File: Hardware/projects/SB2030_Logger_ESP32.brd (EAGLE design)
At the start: 36.5 x 80 mm, 34 parts, among them SW1 CKTACTSWITCH, U1 ESP-WROOM-32, U2 MCP2562, U3 NCP1117ST50T3G, U4 NCP1117ST33T3G, U5 SN65C1168PWR, X1 1751280

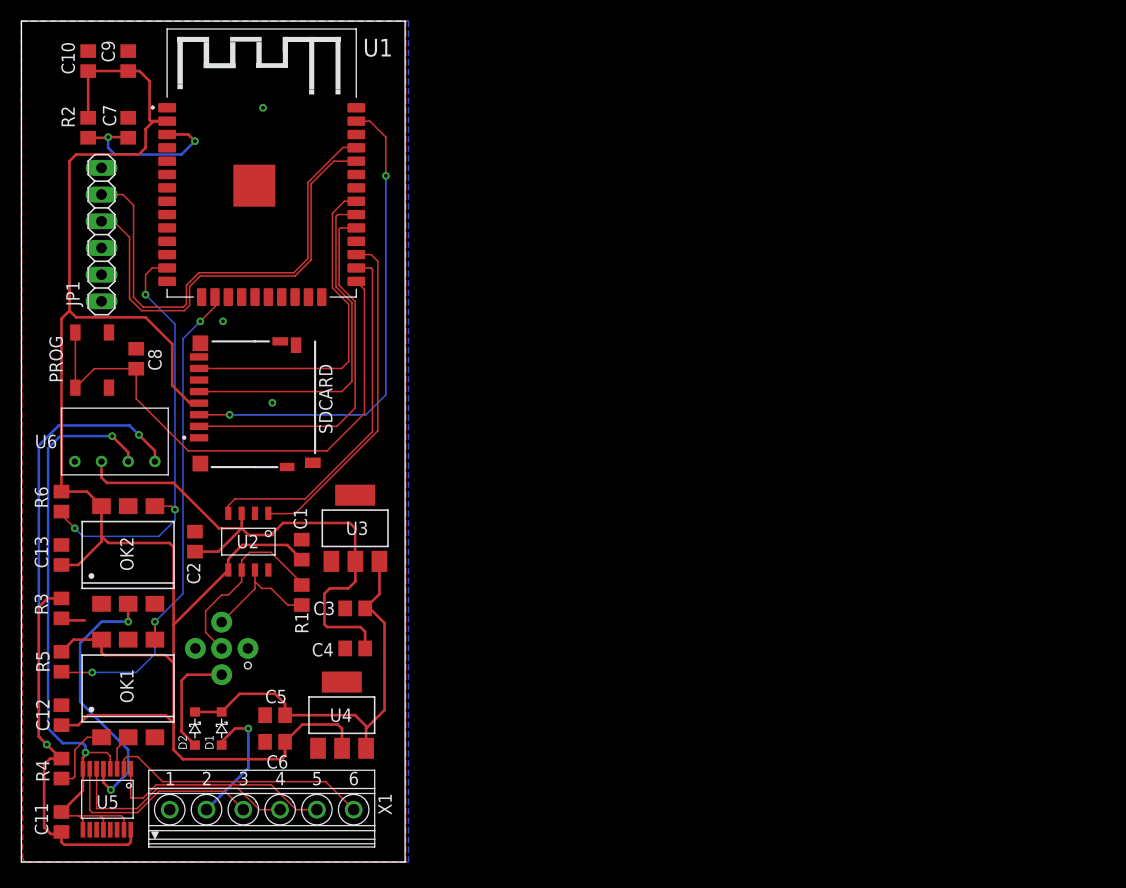
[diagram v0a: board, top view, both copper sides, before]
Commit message: Major updates to SMD board design (added motion sensor and power management), with re-layout for production. Added Gerbers, BOM, and CPL for JLCPCB production. Added library for MPU6050 IMU. Added CCOM logo for silkscreen.
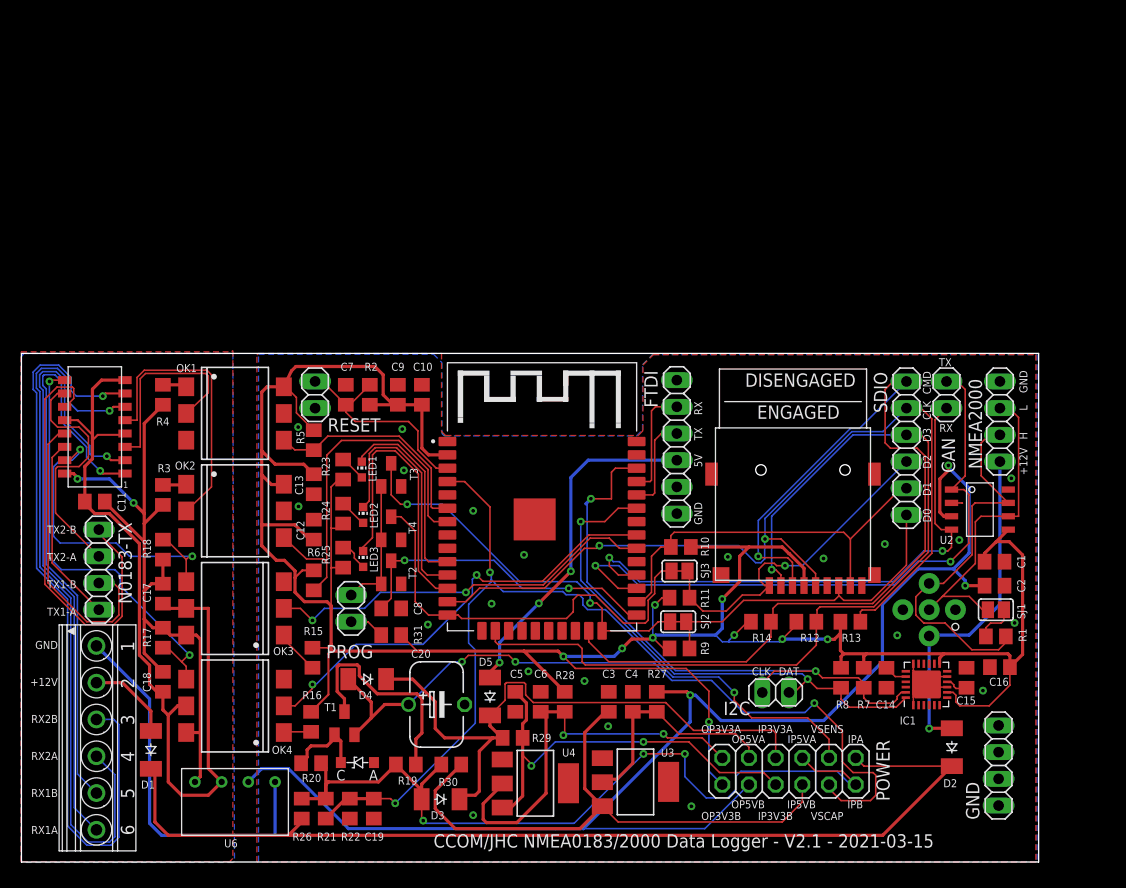
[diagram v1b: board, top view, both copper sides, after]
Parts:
- removed JP1: FTDI/ICSP, pinhead:1X06
- removed SDCARD: MicroSD Holder, 1140084168:1140084168
- removed SW1: CKTACTSWITCH, sb2030_logger:CKTACTSWITCH
- added C14: 2n2, rcl:C0805
- added C15, C17, C18, C19: 0.1u, rcl:C0805
- added C16: 10n, rcl:C0805
- added C20: 0.47F, rcl:P128-50
- added CAN: CAN-TEST, pinhead:1X02
- added D3, D4, D5: SS14, diode:SOD-123_MINI-SMA
- added DZL4734: (no value), sb2030_logger:SOD-123FL
- added FTDI: FTDI/ICSP, pinhead:1X06
- added GND: (no value), pinhead:1X04
- added I2C: I2C_TEST, pinhead:1X02
- added IC1: MPU6050, invensense:QFN50P400X400X95-25T265X275N
- added LED1, LED2, LED3: (no value), led:CHIP-LED0603
- added N0183-TX: TX_TEST, pinhead:1X04
- added NMEA2000: NMEA2000-2, pinhead:1X04
- added OK3, OK4: H11L1MS, optocoupler:DIL6-SMD
- added POWER: (no value), pinhead:2X06
- added PROG: PROG, pinhead:1X02
- added R10, R11, R12, R13, R14, R9: 47k, rcl:R0805
- added R15, R16: 560, rcl:R0805
- added R17, R18, R22, R7, R8: 10k, rcl:R0805
- added R19: 47R, rcl:R0805
- added R20: 1k, rcl:R0805
- added R21: 33k, rcl:R0805
- added R23, R24, R25: 220, rcl:R0805
- added R26, R27, R28, R29, R30: 1R, rcl:R0805
- added R31: 6k8, rcl:R0805
- added RESET: RESET, pinhead:1X02
- added SDIO: SDIO_TEST, pinhead:1X06
- added SJ1, SJ2, SJ3: (no value), jumper:SJ
- added T1: (no value), transistor:SOT23-BEC
- added T2, T3, T4: S8050, transistor:SOT23
- added U$1: MICRO-SD, sb2030_logger:XUNPU-MICROSD-SOCKET
- D1, D2: value 1N5819 -> SS14; device sb2030_logger:SOD123 -> diode:SOD-123_MINI-SMA
- R3, R4: value 1k2 -> 1k
- U3: value NCP1117ST50T3G -> AMS1117-5.0
- U4: value NCP1117ST33T3G -> AMS1117-3.3
- U5: device sb2030_logger:16-TSSOP -> sb2030_logger:SOIC16
- moved C2 76.2 mm to (92.6, 26.3), turned to 0 degrees
- moved D2 72.0 mm to (88.5, 10.9)
- moved U2 69.7 mm to (91.2, 33.5), turned to 270 degrees
- moved JP2 67.4 mm to (86.4, 24.0)
- moved R1 66.2 mm to (92.7, 21.5), turned to 0 degrees
- moved C1 65.9 mm to (92.6, 28.6), turned to 0 degrees
- moved C10 44.9 mm to (38.1, 44.5)
- moved U1 41.5 mm to (49.5, 31.8)
- moved C9 40.8 mm to (35.8, 44.5)
- moved R2 36.9 mm to (33.1, 44.5), turned to 270 degrees
- moved R4 36.8 mm to (13.5, 44.5), turned to 270 degrees
- moved U5 36.1 mm to (6.99, 42.0), turned to 180 degrees
- moved U3 36.0 mm to (58.4, 7.62), turned to 270 degrees
- moved C8 33.9 mm to (35.2, 24.1), turned to 0 degrees
- moved C7 32.8 mm to (30.9, 44.5)
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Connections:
- removed net VIN: C3.1, C5.1, D1.2, D2.2, U3.3, U4.3
- new net CAN-12V: D2.A, JP2.2, NMEA2000.1
- new net FTDI-5V: D5.A, FTDI.3
- new net IP_CUR_3V3_A: D3.C, D4.C, D5.C, POWER.7, R29.2
- new net IP_CUR_3V3_B: C5.1, POWER.8, R29.1, U4.3
- new net IP_CUR_5V_B: C3.1, POWER.6, R30.1, U3.3
- new net IP_CUR_A: D1.C, D2.C, POWER.1, R26.2
- new net IP_CUR_B: D3.A, POWER.2, POWER.5, R19.2, R20.2, R21.2, R26.1, R30.2
- new net N$11: R10.1, SDIO.2, U$1.8, U1.26
- new net N$23: C14.1, IC1.20
- new net N$24: R12.1, SDIO.4, U$1.2, U1.16
- new net N$25: R13.1, SDIO.5, U$1.5, U1.13
- new net N$26: R14.1, SDIO.6, U$1.3, U1.23
- new net N$27: N0183-TX.4, U5.1Y
- new net N$28: N0183-TX.3, U5.1Z
- new net N$29: N0183-TX.2, U5.2Y
- new net N$3: R1.1, SJ1.2
- new net N$30: N0183-TX.1, U5.2Z
- new net N$31: OK3.1, R15.1
- new net N$32: OK4.1, R16.1
- new net N$33: OK3.4, R18.1, U5.1D
- new net N$34: OK4.4, R17.1, U5.2D
- new net N$35: LED1.C, U1.10
- new net N$36: LED2.C, U1.11
- new net N$37: PROG.2, T2.1, T3.1, T4.1
- new net N$38: LED3.C, U1.12
- new net N$39: LED1.A, R23.2
- new net N$40: LED2.A, R24.2
- new net N$41: DZL4734.K, R20.1, T1.B
- new net N$42: R19.1, T1.C
- new net N$43: PROG.1, R31.1
- new net N$44: LED3.A, R25.2
- new net OP_CUR_3V3_A: C6.1, POWER.11, R28.2, U4.2
- new net OP_CUR_5V_A: C4.1, POWER.9, R27.2, U3.2
- new net SCAP: C20.+, D4.A, POWER.4, T1.E
- new net TX1: OK3.2, U1.30
- new net TX2: OK4.2, U1.31
- new net VSENSE: C19.1, POWER.3, R21.1, R22.2, U1.4
- net +12V: now also D1.A; no longer D1.1
- net +3V3: now also C16.1, IC1.13, IC1.8, POWER.12, R10.2, R11.2, R12.2, R13.2, R14.2, R15.2, R16.2, R23.1, R24.1, R25.1, R28.1, R31.2, R7.2, R8.2, R9.2, U$1.4; no longer C6.1, SDCARD.4, U4.2
- net +5V: now also POWER.10, R27.1; no longer C4.1, U3.2
- net GND: now also C14.2, C15.2, C16.2, C19.2, C20.-, DZL4734.A, FTDI.1, GND.1, GND.2, GND.3, GND.4, IC1.1, IC1.11, IC1.18, IC1.25, IC1.9, NMEA2000.4, R22.1, RESET.2, T2.2, T3.2, T4.2, U$1.6, U$1.GND1, U$1.GND2, U$1.GND3, U$1.GND4; no longer JP1.1, SDCARD.6, SW1.3, SW1.4
- net GNDI: now also C17.2, C18.2, OK3.5, OK4.5, U5.1DE, U5.2DE, U5.GND; no longer U5.12, U5.15, U5.4, U5.8, U5.9
- net N$1: now also NMEA2000.2, R1.2; no longer R1.1
- net N$10: now also R11.1, SDIO.3, SJ3.1, SJ3.2, T4.3, U$1.1, U1.14; no longer SDCARD.7, U1.31
- net N$12: now also T2.3; no longer SW1.1, SW1.2
- net N$13: now also U5.1R; no longer U5.3
- net N$14: now also U5.2R; no longer U5.5
- net N$17: now also U5.1A; no longer U5.2
- net N$18: now also U5.1B; no longer U5.1
- net N$19: now also U5.2A; no longer U5.6
- net N$2: now also NMEA2000.3, SJ1.1; no longer R1.2
- net N$20: now also U5.2B; no longer U5.7
- net N$21: now also C17.1, C18.1, OK3.6, OK4.6, R17.2, R18.2, U5.VCC; no longer U5.16
- net N$22: now also R9.1, SDIO.1, SJ2.1, SJ2.2, T3.3, U$1.7, U1.24; no longer D2.1, JP2.2
- net N$4: now also RESET.1
- net N$5: now also I2C.2, IC1.23, R7.1, U1.36; no longer SDCARD.2, U1.29
- net N$6: now also CAN.2
- net N$7: now also CAN.1, U1.28; no longer U1.26
- net N$8: now also I2C.1, IC1.24, R8.1, U1.33; no longer SDCARD.3, U1.37
- net N$9: now also C15.1, IC1.10; no longer SDCARD.5, U1.30
- net RX1: now also U1.6; no longer U1.16
- net RX2: now also U1.7; no longer U1.13
- net RXDATA: now also FTDI.5; no longer JP1.5
- net TXDATA: now also FTDI.4; no longer JP1.4
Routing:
- net IP_CUR_A: track 0.00 -> 95.9 mm
- net +3V3: track 178.4 -> 272.7 mm, vias 0 -> 9
- net N$26: track 0.00 -> 89.1 mm, vias 0 -> 1
- net N$25: track 0.00 -> 87.9 mm, vias 0 -> 2
- net N$24: track 0.00 -> 86.3 mm, vias 0 -> 1
- net VSENSE: track 0.00 -> 86.2 mm, vias 0 -> 3
- net IP_CUR_B: track 0.00 -> 80.6 mm, vias 0 -> 3
- net +5V: track 52.6 -> 131.6 mm, vias 0 -> 3
- net SCAP: track 0.00 -> 71.9 mm, vias 0 -> 3
- net N$22: track 10.7 -> 70.5 mm, vias 0 -> 2
- net IP_CUR_3V3_A: track 0.00 -> 59.6 mm
- net IP_CUR_5V_B: track 0.00 -> 55.7 mm
- net N$20: track 20.2 -> 74.6 mm, vias 0 -> 1
- net GND: track 0.00 -> 48.5 mm, vias 3 -> 21
- net N$19: track 22.9 -> 69.5 mm, vias 0 -> 1
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- added copper zone on layer 1, net GNDI
- added copper zone on layer 16, net GNDI
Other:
- board size 36.5 x 80 mm -> 96.8 x 48.4 mm
- board text added: "(c) 2021 Center for Coastal and Ocean Mapping University of New Hampshire 2021-03-15 V2.1"
- board text added: "+12V"
- board text added: "5V"
- board text added: "CCOM/JHC NMEA0183/2000 Data Logger - V2.1 - 2021-03-15"
- board text added: "CLK"
- board text added: "CMD"
- board text added: "D0"
- board text added: "D1"
- board text added: "D2"
- board text added: "D3"
- board text added: "DAT"
- board text added: "GND"
- board text added: "H"
- board text added: "IP3V3A"
- board text added: "IP3V3B"
- board text added: "IP5VA"
- board text added: "IP5VB"
- board text added: "IPA"
- board text added: "IPB"
- board text added: "L"
- board text added: "OP3V3A"
- board text added: "OP3V3B"
- board text added: "OP5VA"
- board text added: "OP5VB"
- board text added: "RX"
- board text added: "RX1A"
- board text added: "RX1B"
- board text added: "RX2A"
- board text added: "RX2B"
- board text added: "TX"
- board text added: "TX1-A"
- board text added: "TX1-B"
- board text added: "TX2-A"
- board text added: "TX2-B"
- board text added: "VSCAP"
- board text added: "VSENS"
- board text removed: "PROG"

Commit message: Re-routed demonstration board to ensure that the power distribution is better.
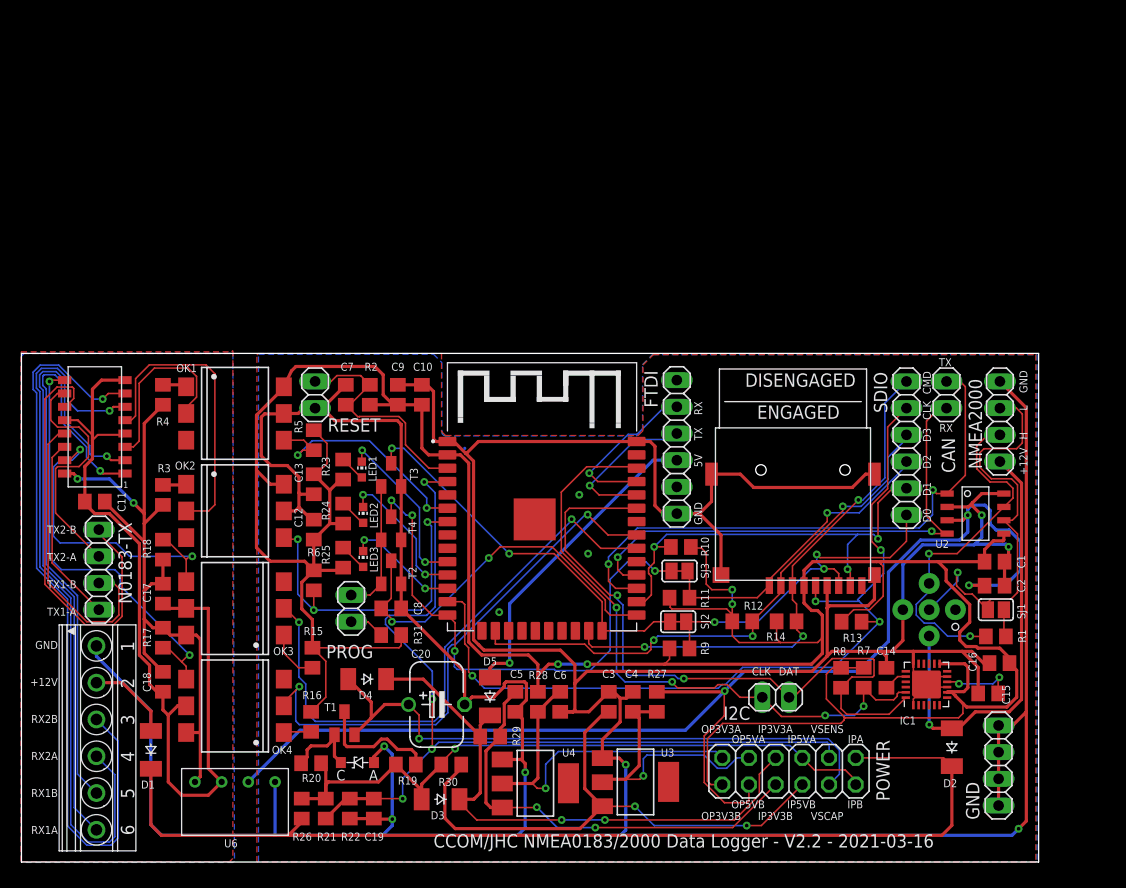
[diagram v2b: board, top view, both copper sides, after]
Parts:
- moved R12 6.10 mm to (68.6, 22.9)
- moved R28 2.55 mm to (49.1, 15.2)
- moved C15 2.54 mm to (92.0, 16.0), turned to 180 degrees
- moved R14 2.44 mm to (72.8, 22.9)
- moved R29 2.14 mm to (44.6, 11.9)
- moved C6 1.85 mm to (51.3, 15.2), turned to 270 degrees
- moved U2 0.57 mm to (90.8, 33.1)
- moved I2C 0.46 mm to (71.8, 15.7)
- moved C16 0.38 mm to (93.1, 18.9)
- moved R13 0.11 mm to (79.0, 22.9)
- turned C14 to 90 degrees
- turned R1 to 180 degrees
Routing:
- net GND: track 48.5 -> 497.2 mm, vias 21 -> 10
- net N$26: track 89.1 -> 51.6 mm, vias 1 -> 3
- net N$24: track 86.3 -> 53.4 mm, vias 1 -> 3
- net +3V3: track 272.7 -> 301.8 mm, vias 9 -> 4
- net TX1: track 37.7 -> 55.4 mm
- net N$38: track 27.6 -> 10.9 mm, vias 0 -> 2
- net IP_CUR_B: track 80.6 -> 65.2 mm, vias 3 -> 1
- net N$8: track 50.7 -> 65.3 mm
- net SCAP: track 71.9 -> 58.7 mm, vias 3 -> 1
- net N$2: track 30.9 -> 40.8 mm, vias 0 -> 1
- net CAN-12V: track 32.5 -> 42.2 mm
- net N$36: track 23.4 -> 13.9 mm, vias 0 -> 2
- net TX2: track 41.9 -> 51.1 mm
- net N$42: track 21.0 -> 11.9 mm
- net N$6: track 61.4 -> 54.5 mm
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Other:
- board text added: "CCOM/JHC NMEA0183/2000 Data Logger - V2.2 - 2021-03-16"
- board text removed: "CCOM/JHC NMEA0183/2000 Data Logger - V2.1 - 2021-03-15"

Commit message: Updates to library specifications for devices, and schematic/board to match in order to give better match to actual components; V2.3 of demonstration board.
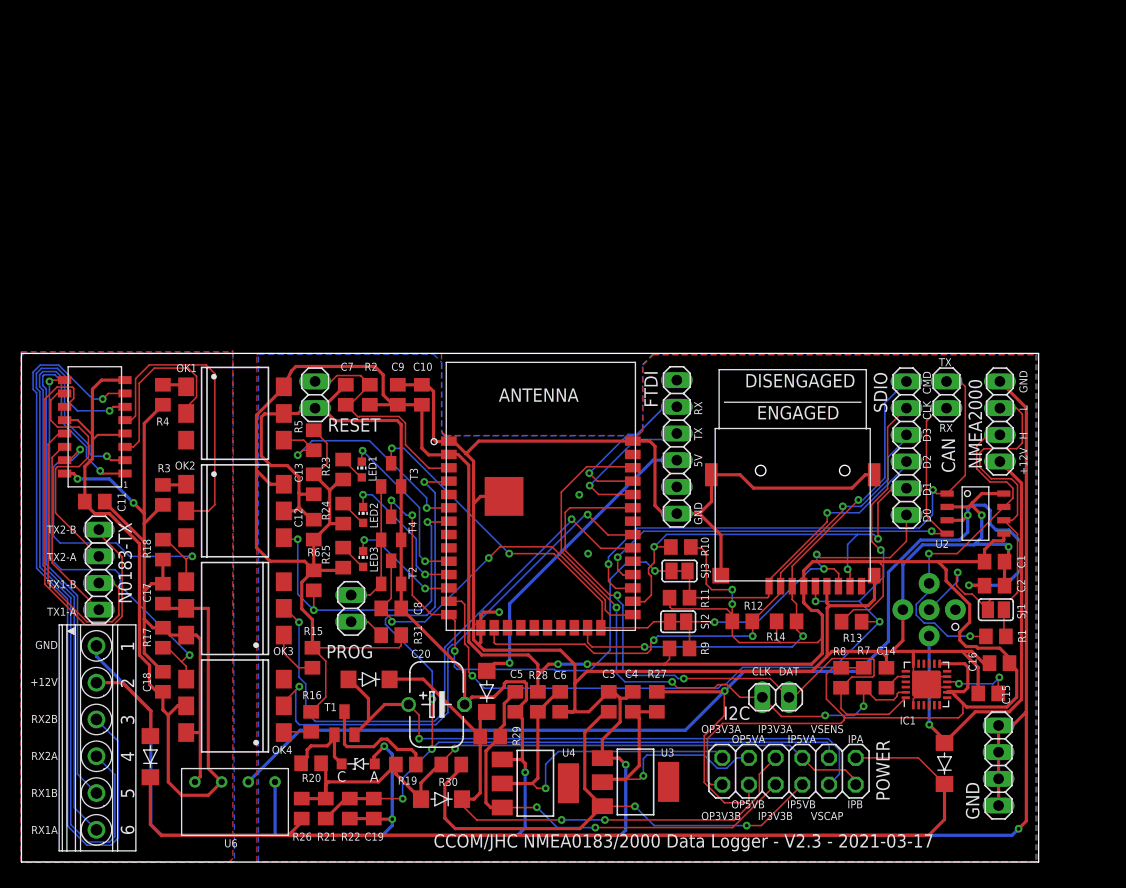
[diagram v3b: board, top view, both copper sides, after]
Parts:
- removed DZL4734: (no value), sb2030_logger:SOD-123FL
- removed U$1: MICRO-SD, sb2030_logger:XUNPU-MICROSD-SOCKET
- added H1: TF-115, sb2030_logger:XUNPU-MICROSD-SOCKET
- added Z1: DZL4734, sb2030_logger:SOD-123FL
- D1, D2, D3, D4, D5: device diode:SOD-123_MINI-SMA -> sb2030_logger:DO-214AC
- U1: value ESP-WROOM-32 -> ESP32-WROOM-32E; device ESP-WROOM-32:MODULE_ESP-WROOM-32 -> sb2030_logger:ESPS32-WROOM-32E
- U2: value MCP2562 -> TLA1051T/3
- moved U1 3.04 mm to (49.4, 34.8)
- moved D2 1.70 mm to (87.8, 9.37)
- moved D1 0.65 mm to (12.3, 10.0)
- moved D5 0.57 mm to (44.3, 16.2)
- moved D4 0.18 mm to (33.1, 17.4)
- moved D3 0.09 mm to (40.0, 5.98)
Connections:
- net +3V3: now also H1.4; no longer U$1.4
- net GND: now also H1.6, H1.GND1, H1.GND2, H1.GND3, H1.GND4, U1.THERM, Z1.A; no longer DZL4734.A, U$1.6, U$1.GND1, U$1.GND2, U$1.GND3, U$1.GND4, U1.1.1
- net IP_CUR_3V3_A: now also D3.K, D4.K, D5.K; no longer D3.C, D4.C, D5.C
- net IP_CUR_A: now also D1.K, D2.K; no longer D1.C, D2.C
- net N$10: now also H1.1; no longer U$1.1
- net N$11: now also H1.8; no longer U$1.8
- net N$22: now also H1.7; no longer U$1.7
- net N$24: now also H1.2; no longer U$1.2
- net N$25: now also H1.5; no longer U$1.5
- net N$26: now also H1.3; no longer U$1.3
- net N$41: now also Z1.K; no longer DZL4734.K
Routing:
- net GND: track 497.2 -> 505.1 mm
- net IP_CUR_A: track 99.6 -> 96.0 mm
- net CAN-12V: track 42.2 -> 43.3 mm
- net N$10: track 81.7 -> 82.4 mm
- net +12V: track 8.19 -> 8.70 mm
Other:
- board text added: "(c) 2021 Center for Coastal and Ocean Mapping University of New Hampshire 2021-03-17 V2.3"
- board text added: "CCOM/JHC NMEA0183/2000 Data Logger - V2.3 - 2021-03-17"
- board text removed: "(c) 2021 Center for Coastal and Ocean Mapping University of New Hampshire 2021-03-15 V2.1"
- board text removed: "CCOM/JHC NMEA0183/2000 Data Logger - V2.2 - 2021-03-16"

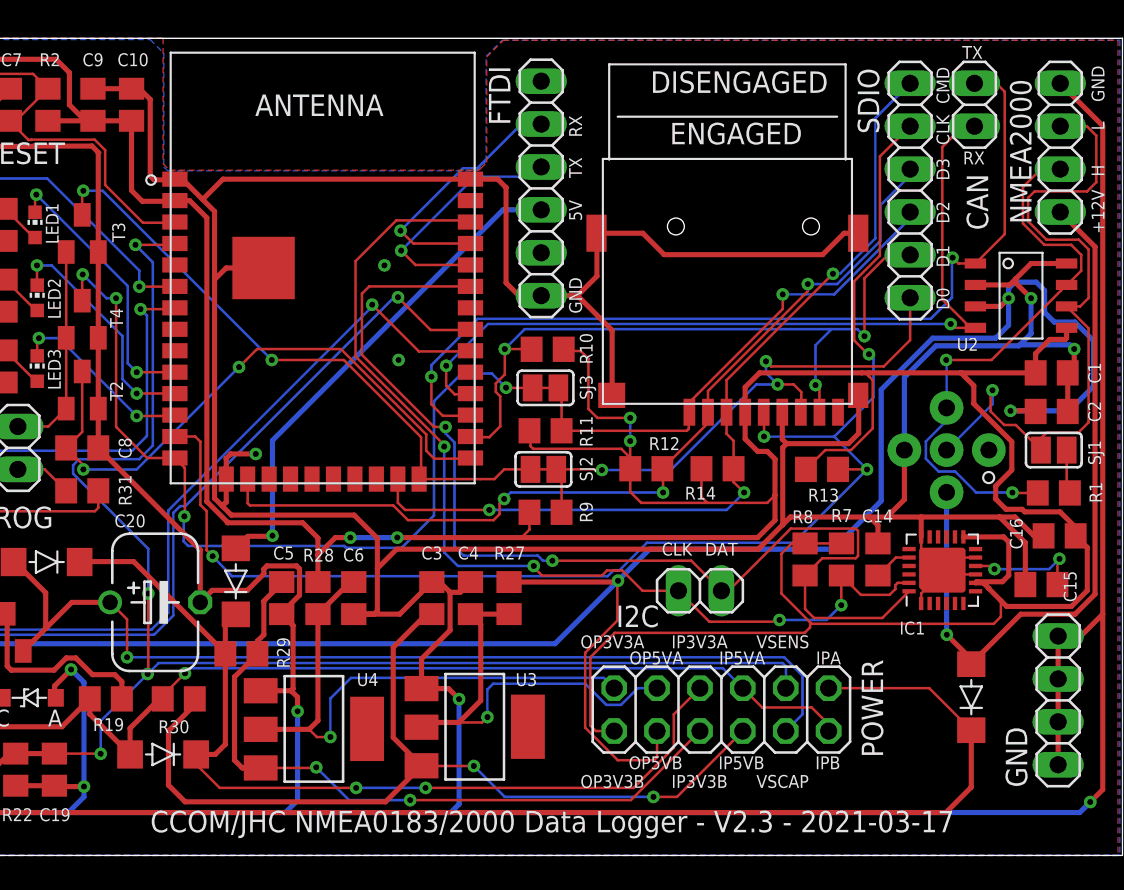
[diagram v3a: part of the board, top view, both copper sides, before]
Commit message: Modifications to PCB layout to improve ground planes, and to attempt to fix centroid problems for ESP32-WROOM-32E
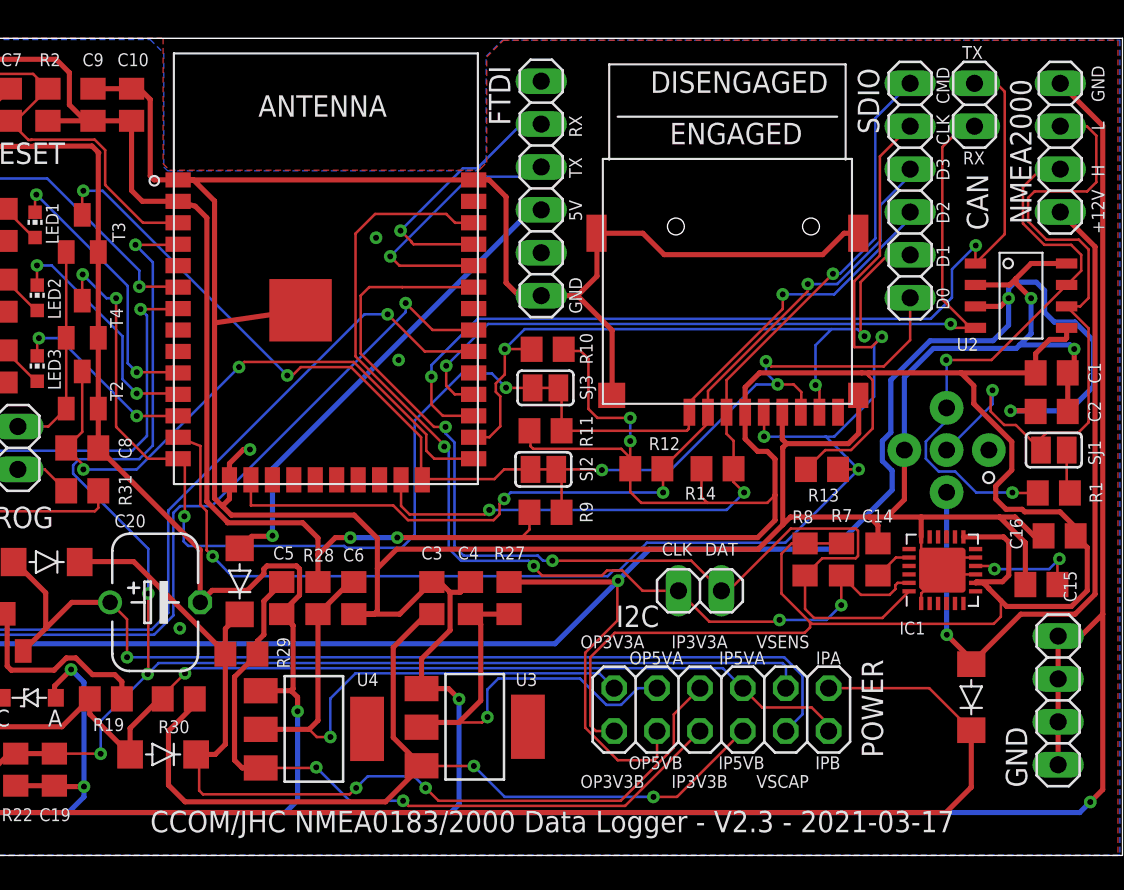
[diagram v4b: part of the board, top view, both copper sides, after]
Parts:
- moved U1 3.13 mm to (49.6, 31.7)
- moved D5 0.23 mm to (44.5, 16.2)
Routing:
- net GND: track 505.1 -> 507.7 mm, vias 10 -> 11
- net IP_CUR_3V3_A: track 55.4 -> 57.8 mm
- net TXDATA: track 14.8 -> 16.3 mm
- net FTDI-5V: track 29.7 -> 28.5 mm
- net N$5: track 59.8 -> 61.0 mm
- net N$6: track 54.2 -> 55.2 mm
- net N$25: track 81.9 -> 82.6 mm
